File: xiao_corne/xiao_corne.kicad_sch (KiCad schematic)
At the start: 79 parts, among them J1 USB4110GFA, J6 Conn_01x04_Socket, SW1 SW_Push, SW11 SW_Push, SW12 SW_Push, SW13 SW_Push, SW14 SW_Push, SW15 SW_Push, SW2 SW_Push, SW21 SW_Push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

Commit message: ready for review
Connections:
- net GND is gone; now on net GND L: U2.1 (GND), U2.40 (GND), U2.41 (GND), U4.4 (CE_N)
- net BAT/2 MON L: no longer U2.39 (GPIO1/TOUCH1/ADC1_CH0)
- no-connect marks 30 -> 32
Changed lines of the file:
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@@
 		)
 	)
+	(circle
+		(center 275.59 270.51)
+		(radius 6.8392)
+		(stroke
+			(width 0)
+			(type default)
+		)
+		(fill
+			(type color)
+			(color 255 0 0 1)
+		)
+	)
 	(rectangle
 		(start 16.51 16.51)
@@
 	)
 	(no_connect
+		(at 273.05 271.78)
+	)
+	(no_connect
+		(at 276.86 271.78)
+	)
+	(no_connect
 		(at 181.61 276.86)
 	)
@@
 	(global_label "BAT{slash}2 MON L"
 		(shape input)
-		(at 273.05 271.78 0)
+		(at 276.86 271.78 0)
 		(fields_autoplaced yes)
 		(effects
@@
 		)
 		(property "Intersheetrefs" "${INTERSHEET_REFS}"
-			(at 288.9771 271.78 0)
+			(at 292.7871 271.78 0)
 			(effects
 				(font
@@
 	)
 	(symbol
+		(lib_id "power:GND")
+		(at 449.58 180.34 270)
+		(unit 1)
+		(exclude_from_sim no)
+		(in_bom yes)
+		(on_board yes)
+		(dnp no)
+		(fields_autoplaced yes)
+		(property "Reference" "#PWR028"
+			(at 443.23 180.34 0)
+			(effects
+				(font
+					(size 1.27 1.27)
+				)
+				(hide yes)
+			)
+		)
+		(property "Value" "GND L"
+			(at 445.77 180.3399 90)
+			(effects
+				(font
+					(size 1.27 1.27)
+				)
+				(justify right)
+			)
+		)
+		(property "Footprint" ""
+			(at 449.58 180.34 0)
+			(effects
+				(font
+					(size 1.27 1.27)
+				)
+				(hide yes)
+			)
+		)
+		(property "Datasheet" ""
+			(at 449.58 180.34 0)
+			(effects
+				(font
+					(size 1.27 1.27)
+				)
+				(hide yes)
+			)
+		)
+		(property "Description" "Power symbol creates a global label with name \"GND\" , ground"
+			(at 449.58 180.34 0)
+			(effects
+				(font
+					(size 1.27 1.27)
+				)
+				(hide yes)
+			)
+		)
+		(pin "1"
+		)
+		(instances
+			(project "xiao_corne"
+				(path "/efa30048-eef2-4d23-8f91-f1f3cca8359e"
+					(reference "#PWR028")
+					(unit 1)
+				)
+			)
+		)
+	)
+	(symbol
 		(lib_id "Device:R")
 		(at 494.03 180.34 270)
@@
 	)
 	(symbol
-		(lib_id "power:GND")
-		(at 227.33 330.2 0)
-		(unit 1)
-		(exclude_from_sim no)
-		(in_bom yes)
-		(on_board yes)
-		(dnp no)
-		(fields_autoplaced yes)
-		(property "Reference" "#PWR017"
-			(at 227.33 336.55 0)
-			(effects
-				(font
-					(size 1.27 1.27)
-				)
-				(hide yes)
-			)
-		)
-		(property "Value" "GND"
-			(at 227.33 335.28 0)
-			(effects
-				(font
-					(size 1.27 1.27)
-				)
-			)
-		)
-		(property "Footprint" ""
-			(at 227.33 330.2 0)
-			(effects
-				(font
-					(size 1.27 1.27)
-				)
-				(hide yes)
-			)
-		)
-		(property "Datasheet" ""
-			(at 227.33 330.2 0)
-			(effects
-				(font
-					(size 1.27 1.27)
-				)
-				(hide yes)
-			)
-		)
-		(property "Description" "Power symbol creates a global label with name \"GND\" , ground"
-			(at 227.33 330.2 0)
-			(effects
-				(font
-					(size 1.27 1.27)
-				)
-				(hide yes)
-			)
-		)
-		(pin "1"
-		)
-		(instances
-			(project "xiao_corne"
-				(path "/efa30048-eef2-4d23-8f91-f1f3cca8359e"
-					(reference "#PWR017")
-					(unit 1)
-				)
-			)
-		)
-	)
-	(symbol
 		(lib_id "ScottoKeebs:LED_SK6812MINI")
 		(at 311.15 73.66 0)
@@
 	)
 	(symbol
+		(lib_id "power:GND")
+		(at 227.33 330.2 0)
+		(unit 1)
+		(exclude_from_sim no)
+		(in_bom yes)
+		(on_board yes)
+		(dnp no)
+		(fields_autoplaced yes)
+		(property "Reference" "#PWR05"
+			(at 227.33 336.55 0)
+			(effects
+				(font
+					(size 1.27 1.27)
+				)
+				(hide yes)
+			)
+		)
+		(property "Value" "GND L"
+			(at 227.33 334.3331 0)
+			(effects
+				(font
+					(size 1.27 1.27)
+				)
+			)
+		)
+		(property "Footprint" ""
+			(at 227.33 330.2 0)
+			(effects
+				(font
+					(size 1.27 1.27)
+				)
+				(hide yes)
+			)
+		)
+		(property "Datasheet" ""
+			(at 227.33 330.2 0)
+			(effects
+				(font
+					(size 1.27 1.27)
+				)
+				(hide yes)
+			)
+		)
+		(property "Description" "Power symbol creates a global label with name \"GND\" , ground"
+			(at 227.33 330.2 0)
+			(effects
+				(font
+					(size 1.27 1.27)
+				)
+				(hide yes)
+			)
+		)
+		(pin "1"
+		)
+		(instances
+			(project "xiao_corne"
+				(path "/efa30048-eef2-4d23-8f91-f1f3cca8359e"
+					(reference "#PWR05")
+					(unit 1)
+				)
+			)
+		)
+	)
+	(symbol
 		(lib_id "Device:R")
 		(at 350.52 259.08 270)
@@
 					(unit 1)
 				)
-			)
-		)
-	)
-	(symbol
-		(lib_id "power:GND")
-		(at 449.58 180.34 270)
-		(unit 1)
-		(exclude_from_sim no)
-		(in_bom yes)
-		(on_board yes)
-		(dnp no)
-		(fields_autoplaced yes)
-		(property "Reference" "#PWR028"
-			(at 443.23 180.34 0)
-			(effects
-				(font
-					(size 1.27 1.27)
-				)
-				(hide yes)
-			)
-		)
-		(property "Value" "GND"
-			(at 445.77 180.3399 90)
-			(effects
-				(font
-					(size 1.27 1.27)
-				)
-				(justify right)
-			)
-		)
-		(property "Footprint" ""
-			(at 449.58 180.34 0)
-			(effects
-				(font
-					(size 1.27 1.27)
-				)
-				(hide yes)
-			)
-		)
-		(property "Datasheet" ""
-			(at 449.58 180.34 0)
-			(effects
-				(font
-					(size 1.27 1.27)
-				)
-				(hide yes)
-			)
-		)
-		(property "Description" "Power symbol creates a global label with name \"GND\" , ground"
-			(at 449.58 180.34 0)
-			(effects
-				(font
-					(size 1.27 1.27)
-				)
-				(hide yes)
-			)
-		)
-		(pin "1"
-		)
-		(instances
-			(project "xiao_corne"
-				(path "/efa30048-eef2-4d23-8f91-f1f3cca8359e"
-					(reference "#PWR028")
-					(unit 1)
-				)

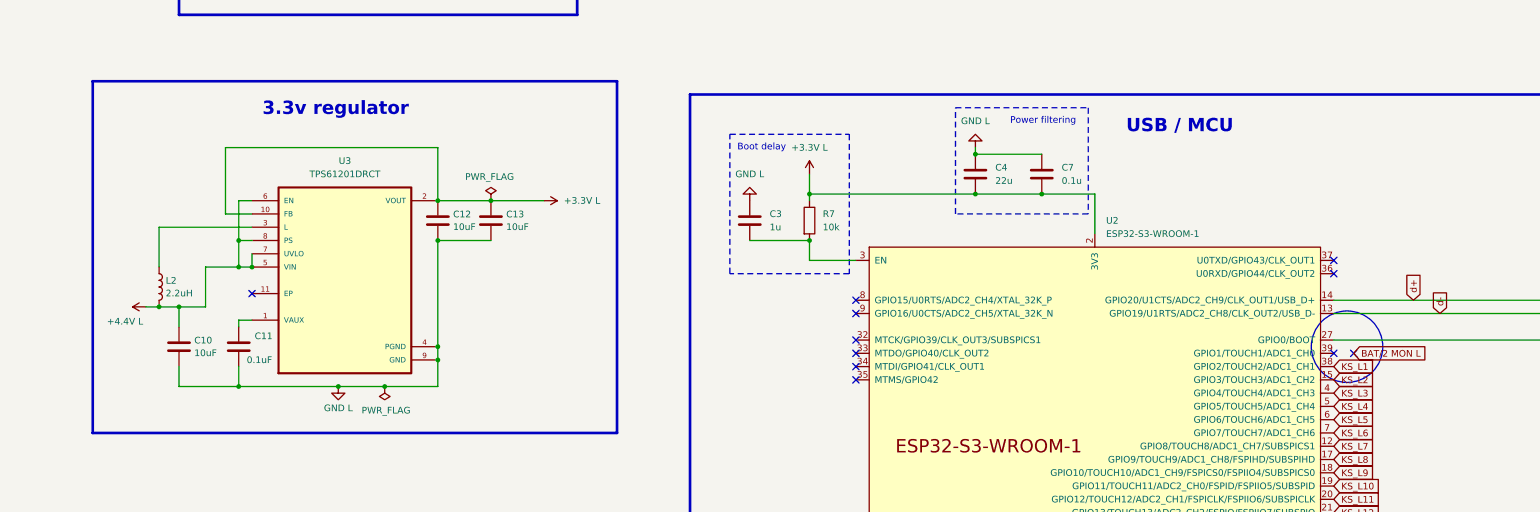
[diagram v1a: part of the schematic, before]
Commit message: changed 3.3v regulator to step down from step up converter
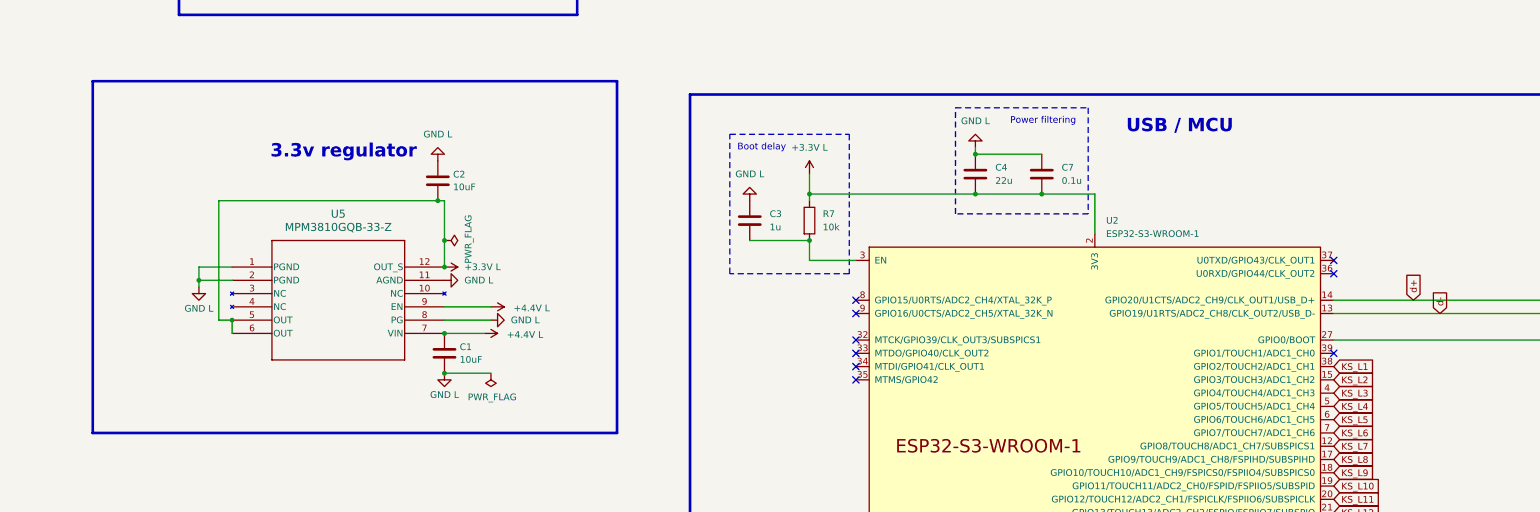
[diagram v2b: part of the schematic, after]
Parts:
- removed C10, C12, C13: 10uF, Capacitor_SMD:C_0805_2012Metric, symbol Device:C
- removed C11: 0.1uF, Capacitor_SMD:C_0805_2012Metric, symbol Device:C
- removed L2: 2.2uH, Inductor_SMD:L_0805_2012Metric, symbol Device:L
- removed U3: TPS61201DRCT, TPS61201DRCT:VREG_V62_16624-01YE, symbol TPS61201DRCT:TPS61201DRCT
- added C1, C2: 10uF, Capacitor_SMD:C_0805_2012Metric, symbol Device:C
- added U5: MPM3810GQB-33-Z, footprints_mpm:QFN-12_MPM3810_MNP, symbol 2026-02-27_05-28-05:MPM3810GQB-33-Z
- SW6: footprint footprints:MJTP1117 -> MJTP1117:MJTP1117
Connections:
- net +3.3V L: now also C2.1, U5.12 (OUT_S), U5.5 (OUT), U5.6 (OUT)
- net +4.4V L: now also C1.2, U5.7 (VIN), U5.9 (EN)
- net GND L: now also C1.1, C2.2, U5.1 (PGND), U5.11 (AGND), U5.2 (PGND), U5.8 (PG)
- no-connect marks 32 -> 30

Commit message: ordered!
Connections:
- net GND L: no longer U5.8 (PG)
- no-connect marks 30 -> 31
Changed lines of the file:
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@@
 			(width 0.508)
 			(type solid)
-			(color 255 153 0 1)
+			(color 0 194 0 1)
 		)
 		(fill
@@
 	)
 	(no_connect
+		(at 102.87 265.43)
+	)
+	(no_connect
 		(at 219.71 166.37)
 	)
@@
 	(wire
 		(pts
-			(xy 102.87 265.43) (xy 111.76 265.43)
-		)
-		(stroke
-			(width 0)
-			(type default)
-		)
-	)
-	(wire
-		(pts
 			(xy 190.5 92.71) (xy 190.5 66.04)
 		)
@@
 					(unit 1)
 				)
-			)
-		)
-	)
-	(symbol
-		(lib_id "power:GND")
-		(at 111.76 265.43 90)
-		(unit 1)
-		(exclude_from_sim no)
-		(in_bom yes)
-		(on_board yes)
-		(dnp no)
-		(fields_autoplaced yes)
-		(property "Reference" "#PWR056"
-			(at 118.11 265.43 0)
-			(effects
-				(font
-					(size 1.27 1.27)
-				)
-				(hide yes)
-			)
-		)
-		(property "Value" "GND L"
-			(at 115.57 265.4299 90)
-			(effects
-				(font
-					(size 1.27 1.27)
-				)
-				(justify right)
-			)
-		)
-		(property "Footprint" ""
-			(at 111.76 265.43 0)
-			(effects
-				(font
-					(size 1.27 1.27)
-				)
-				(hide yes)
-			)
-		)
-		(property "Datasheet" ""
-			(at 111.76 265.43 0)
-			(effects
-				(font
-					(size 1.27 1.27)
-				)
-				(hide yes)
-			)
-		)
-		(property "Description" "Power symbol creates a global label with name \"GND\" , ground"
-			(at 111.76 265.43 0)
-			(effects
-				(font
-					(size 1.27 1.27)
-				)
-				(hide yes)
-			)
-		)
-		(pin "1"
-		)
-		(instances
-			(project "xiao_corne"
-				(path "/efa30048-eef2-4d23-8f91-f1f3cca8359e"
-					(reference "#PWR056")
-					(unit 1)
-				)

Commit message: Fixed issue with battery monitor
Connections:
- net BAT/2 MON L: now also U2.39 (GPIO1/TOUCH1/ADC1_CH0); no longer U2.29 (SPIIO7/GPIO36/FSPICLK/SUBSPICLK)
